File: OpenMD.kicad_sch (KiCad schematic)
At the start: 27 parts, among them J1 GND, J2 Digital, J3 Analog, J5 A, J6 B, J7 C, J8 V_{BATT}

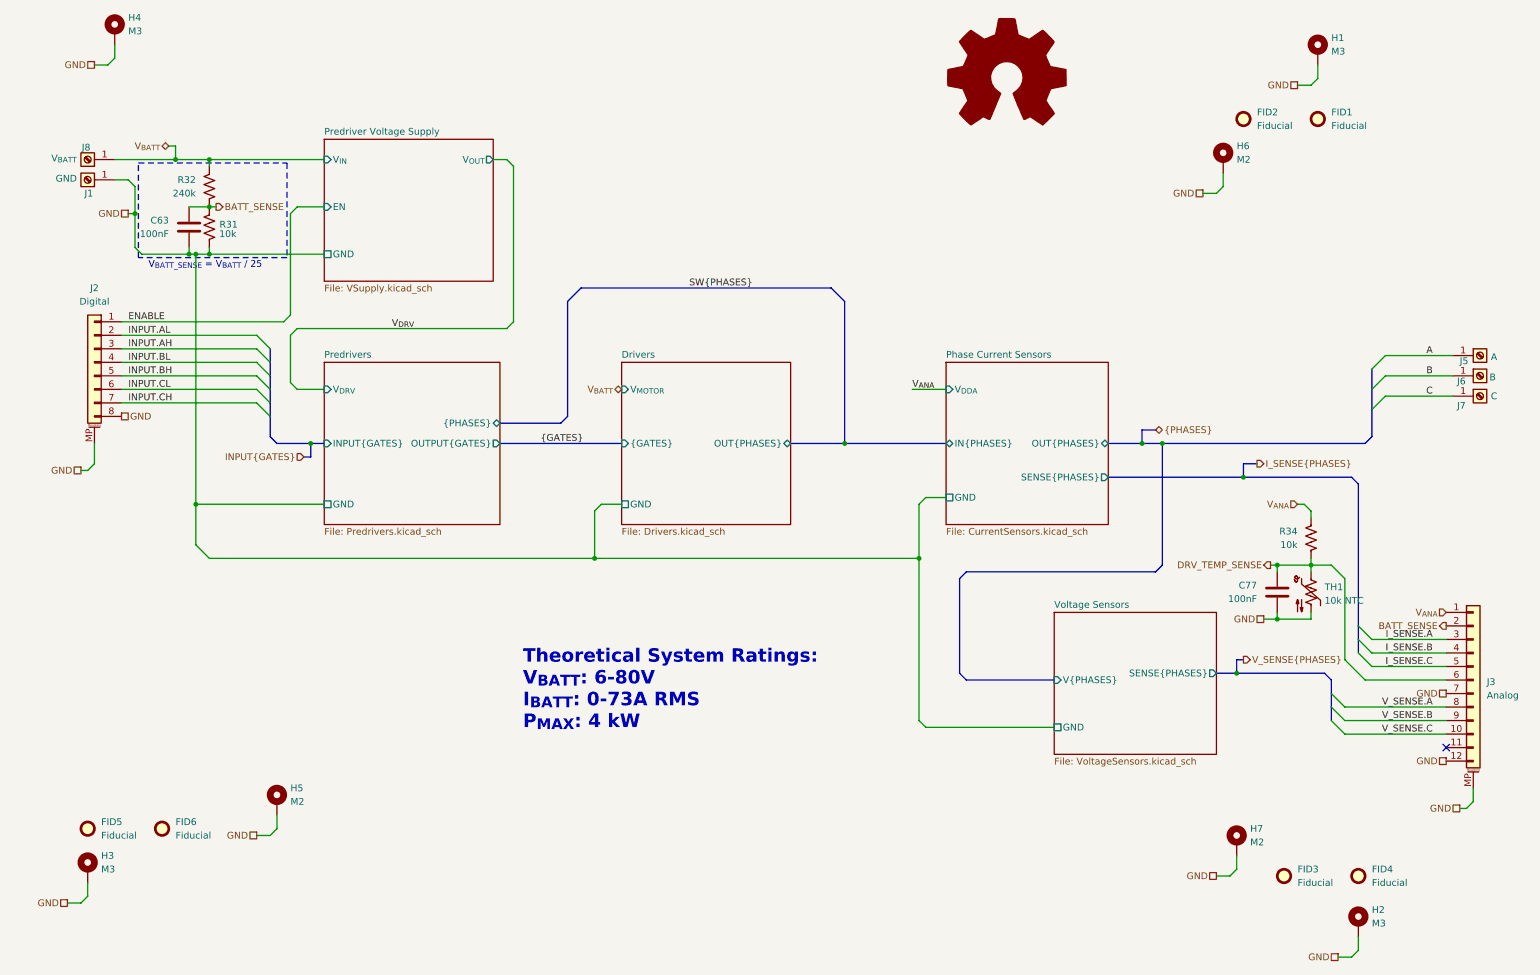
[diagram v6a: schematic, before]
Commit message: added more capacitance
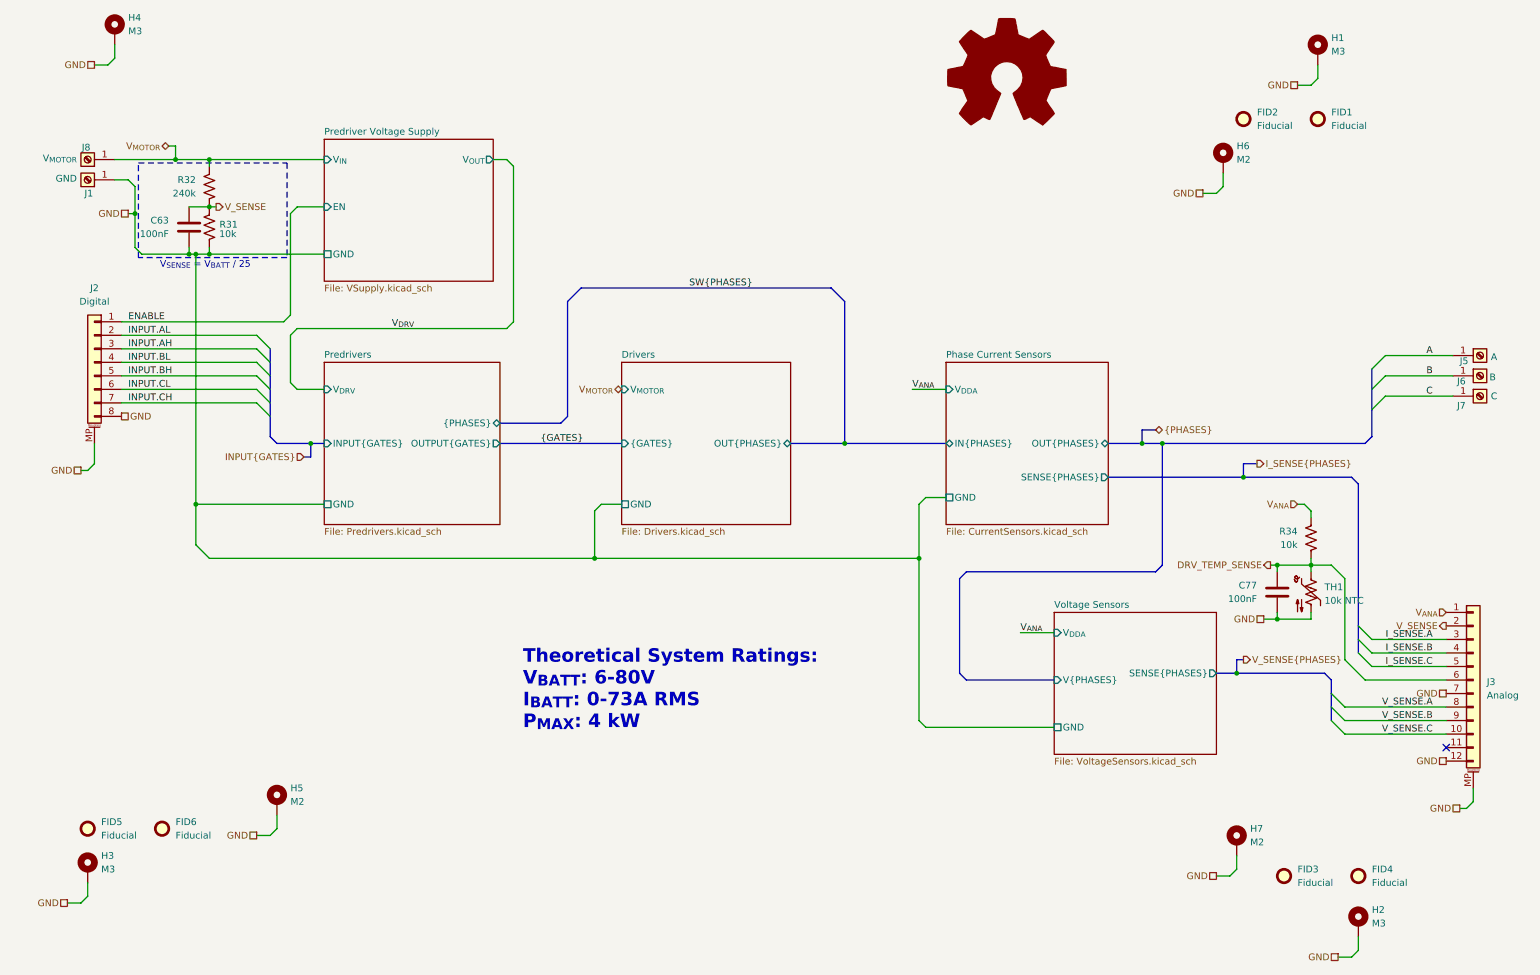
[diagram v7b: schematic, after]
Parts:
- C63, C77: footprint Capacitor_SMD:C_0402_1005Metric -> OpenMD:C_0402_1005Metric; symbol Device:C -> OpenMD:C
- FID1, FID2, FID3, FID4, FID5, FID6: symbol Mechanical:Fiducial -> OpenMD:Fiducial
- H1, H2, H3, H4, H5, H6, H7: symbol Mechanical:MountingHole_Pad -> OpenMD:MountingHole_Pad
- J1, J5, J6, J7: symbol Connector:Screw_Terminal_01x01 -> OpenMD:Screw_Terminal_01x01
- J2: footprint Connector_JST:JST_SH_SM08B-SRSS-TB_1x08-1MP_P1.00mm_Horizontal -> OpenMD:JST_SH_SM08B-SRSS-TB_1x08-1MP_P1.00mm_Horizontal; symbol Connector_Generic_MountingPin:Conn_01x08_MountingPin -> OpenMD:Conn_01x08_MountingPin
- J3: footprint Connector_JST:JST_SH_SM12B-SRSS-TB_1x12-1MP_P1.00mm_Horizontal -> OpenMD:JST_SH_SM12B-SRSS-TB_1x12-1MP_P1.00mm_Horizontal; symbol Connector_Generic_MountingPin:Conn_01x12_MountingPin -> OpenMD:Conn_01x12_MountingPin
- J8: value V_{BATT} -> V_{MOTOR}; symbol Connector:Screw_Terminal_01x01 -> OpenMD:Screw_Terminal_01x01
- R31, R32, R34: footprint Resistor_SMD:R_0402_1005Metric -> OpenMD:R_0402_1005Metric; symbol Device:R_US -> OpenMD:R_US
- SYM1: footprint Symbol:OSHW-Symbol_8.9x8mm_SilkScreen -> Symbol:OSHW-Logo2_7.3x6mm_SilkScreen; symbol Graphic:Logo_Open_Hardware_Large -> OpenMD:Logo_Open_Hardware_Large
- TH1: footprint Resistor_SMD:R_0402_1005Metric -> OpenMD:R_0402_1005Metric; symbol Device:Thermistor_NTC_US -> OpenMD:Thermistor_NTC_US
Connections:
- net BATT_SENSE renamed V_SENSE
- net V_{BATT} renamed V_{MOTOR}
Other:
- sheet Voltage Sensors ports: added V_{DDA}; removed none
- note added: "V_{SENSE} = V_{BATT} / 25"
- note removed: "V_{BATT_SENSE} = V_{BATT} / 25"
- title: 3 Phase Motor Driver -> OpenMD
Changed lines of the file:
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@@
 	(paper "A3")
 	(title_block
-		(title "3 Phase Motor Driver")
-		(date "2024-05-19")
-		(rev "1")
+		(title "OpenMD")
+		(date "2024-12-19")
+		(rev "1.1")
 		(company "Crab Labs")
 		(comment 1 "Author: Orion Serup")
@@
 	(wire
 		(pts
+			(xy 269.24 157.48) (xy 275.59 157.48)
+		)
+		(stroke
+			(width 0)
+			(type default)
+		)
+	)
+	(wire
+		(pts
 			(xy 114.3 133.35) (xy 114.3 140.97)
 		)
@@
 		)
 	)
-	(text "V_{BATT_SENSE} = V_{BATT} / 25\n"
+	(text "V_{SENSE} = V_{BATT} / 25\n"
 		(exclude_from_sim no)
 		(at 116.078 88.392 0)
@@
 		)
 	)
+	(label "V_{ANA}"
+		(at 269.24 157.48 0)
+		(fields_autoplaced yes)
+		(effects
+			(font
+				(size 1.27 1.27)
+			)
+			(justify left bottom)
+		)
+	)
 	(label "V_SENSE.A"
 		(at 346.71 171.45 180)
@@
 		)
 	)
-	(hierarchical_label "V_{BATT}"
+	(hierarchical_label "V_{MOTOR}"
 		(shape bidirectional)
 		(at 194.31 111.76 180)
@@
 		)
 	)
-	(hierarchical_label "BATT_SENSE"
+	(hierarchical_label "V_SENSE"
 		(shape output)
 		(at 349.25 156.21 180)
@@
 		)
 	)
-	(hierarchical_label "BATT_SENSE"
+	(hierarchical_label "V_SENSE"
 		(shape output)
 		(at 118.11 77.47 0)
@@
 		)
 	)
-	(hierarchical_label "V_{BATT}"
+	(hierarchical_label "V_{MOTOR}"
 		(shape bidirectional)
 		(at 109.22 66.04 180)
@@
 	)
 	(symbol
-		(lib_id "Device:R_US")
+		(lib_id "OpenMD:R_US")
 		(at 116.84 73.66 0)
 		(mirror y)
@@
 			)
 		)
-		(property "Footprint" "Resistor_SMD:R_0402_1005Metric"
+		(property "Footprint" "OpenMD:R_0402_1005Metric"
 			(at 115.824 73.914 90)
 			(effects
@@
 	)
 	(symbol
-		(lib_id "Device:C")
+		(lib_id "OpenMD:C")
 		(at 317.5 149.86 0)
 		(mirror y)
@@
 			)
 		)
-		(property "Footprint" "Capacitor_SMD:C_0402_1005Metric"
+		(property "Footprint" "OpenMD:C_0402_1005Metric"
 			(at 316.5348 153.67 0)
 			(effects
@@
 	)
 	(symbol
-		(lib_id "Graphic:Logo_Open_Hardware_Large")
+		(lib_id "OpenMD:Logo_Open_Hardware_Large")
 		(at 266.7 53.34 0)
 		(unit 1)
@@
 			)
 		)
-		(property "Footprint" "Symbol:OSHW-Symbol_8.9x8mm_SilkScreen"
+		(property "Footprint" "Symbol:OSHW-Logo2_7.3x6mm_SilkScreen"
 			(at 266.7 53.34 0)
 			(effects
@@
 	)
 	(symbol
-		(lib_id "Mechanical:MountingHole_Pad")
+		(lib_id "OpenMD:MountingHole_Pad")
 		(at 93.98 201.93 0)
 		(unit 1)
@@
 	)
 	(symbol
-		(lib_id "Mechanical:MountingHole_Pad")
+		(lib_id "OpenMD:MountingHole_Pad")
 		(at 325.12 48.26 0)
 		(unit 1)
@@
 	)
 	(symbol
-		(lib_id "Mechanical:Fiducial")
+		(lib_id "OpenMD:Fiducial")
 		(at 93.98 194.31 0)
 		(unit 1)
@@
 	)
 	(symbol
-		(lib_id "Connector:Screw_Terminal_01x01")
+		(lib_id "OpenMD:Screw_Terminal_01x01")
 		(at 93.98 72.39 180)
 		(unit 1)
@@
 	)
 	(symbol
-		(lib_id "Connector:Screw_Terminal_01x01")
+		(lib_id "OpenMD:Screw_Terminal_01x01")
 		(at 355.6 105.41 0)
 		(unit 1)
@@
 	)
 	(symbol
-		(lib_id "Connector_Generic_MountingPin:Conn_01x08_MountingPin")
+		(lib_id "OpenMD:Conn_01x08_MountingPin")
 		(at 95.25 106.68 0)
 		(mirror y)
@@
 			)
 		)
-		(property "Footprint" "Connector_JST:JST_SH_SM08B-SRSS-TB_1x08-1MP_P1.00mm_Horizontal"
+		(property "Footprint" "OpenMD:JST_SH_SM08B-SRSS-TB_1x08-1MP_P1.00mm_Horizontal"
 			(at 95.25 106.68 0)
 			(effects
@@
 	)
 	(symbol
-		(lib_id "Mechanical:MountingHole_Pad")
+		(lib_id "OpenMD:MountingHole_Pad")
 		(at 332.74 212.09 0)
 		(unit 1)
@@
 	)
 	(symbol
-		(lib_id "Mechanical:Fiducial")
+		(lib_id "OpenMD:Fiducial")
 		(at 311.15 60.96 0)
 		(unit 1)
@@
 	)
 	(symbol
-		(lib_id "Mechanical:Fiducial")
+		(lib_id "OpenMD:Fiducial")
 		(at 325.12 60.96 0)
 		(unit 1)
@@
 	)
 	(symbol
-		(lib_id "Connector_Generic_MountingPin:Conn_01x12_MountingPin")
+		(lib_id "OpenMD:Conn_01x12_MountingPin")
 		(at 354.33 166.37 0)
 		(unit 1)
@@
 			)
 		)
-		(property "Footprint" "Connector_JST:JST_SH_SM12B-SRSS-TB_1x12-1MP_P1.00mm_Horizontal"
+		(property "Footprint" "OpenMD:JST_SH_SM12B-SRSS-TB_1x12-1MP_P1.00mm_Horizontal"
 			(at 354.33 166.37 0)
 			(effects
@@
 	)
 	(symbol
-		(lib_id "Device:R_US")
+		(lib_id "OpenMD:R_US")
 		(at 116.84 81.28 0)
 		(mirror y)
@@
 			)
 		)
-		(property "Footprint" "Resistor_SMD:R_0402_1005Metric"
+		(property "Footprint" "OpenMD:R_0402_1005Metric"
 			(at 115.824 81.534 90)
 			(effects
@@
 	)
 	(symbol
-		(lib_id "Device:R_US")
+		(lib_id "OpenMD:R_US")
 		(at 323.85 139.7 0)
 		(mirror y)
@@
 			)
 		)
-		(property "Footprint" "Resistor_SMD:R_0402_1005Metric"
+		(property "Footprint" "OpenMD:R_0402_1005Metric"
 			(at 322.834 139.954 90)
 			(effects
@@
 	)
 	(symbol
-		(lib_id "Mechanical:Fiducial")
+		(lib_id "OpenMD:Fiducial")
 		(at 107.95 194.31 0)
 		(unit 1)
@@
 	)
 	(symbol
-		(lib_id "Mechanical:MountingHole_Pad")
+		(lib_id "OpenMD:MountingHole_Pad")
 		(at 129.54 189.23 0)
 		(unit 1)
@@
 	)
 	(symbol
-		(lib_id "Mechanical:MountingHole_Pad")
+		(lib_id "OpenMD:MountingHole_Pad")
 		(at 307.34 68.58 0)
 		(unit 1)
@@
 	)
 	(symbol
-		(lib_id "Device:Thermistor_NTC_US")
+		(lib_id "OpenMD:Thermistor_NTC_US")
 		(at 323.85 149.86 0)
 		(unit 1)
@@
 			)
 		)
-		(property "Footprint" "Resistor_SMD:R_0402_1005Metric"
+		(property "Footprint" "OpenMD:R_0402_1005Metric"
 			(at 323.85 148.59 0)
 			(effects
@@
 	)
 	(symbol
-		(lib_id "Mechanical:Fiducial")
+		(lib_id "OpenMD:Fiducial")
 		(at 332.74 203.2 0)
 		(unit 1)
@@
 	)
 	(symbol
-		(lib_id "Mechanical:Fiducial")
+		(lib_id "OpenMD:Fiducial")
 		(at 318.77 203.2 0)
 		(unit 1)
@@
 	)
 	(symbol
-		(lib_id "Connector:Screw_Terminal_01x01")
+		(lib_id "OpenMD:Screw_Terminal_01x01")
 		(at 355.6 109.22 0)
 		(unit 1)
@@
 	)
 	(symbol
-		(lib_id "Mechanical:MountingHole_Pad")
+		(lib_id "OpenMD:MountingHole_Pad")
 		(at 309.88 196.85 0)
 		(unit 1)
@@
 	)
 	(symbol
-		(lib_id "Connector:Screw_Terminal_01x01")
+		(lib_id "OpenMD:Screw_Terminal_01x01")
 		(at 93.98 68.58 180)
 		(unit 1)
@@
 			)
 		)
-		(property "Value" "V_{BATT}"
+		(property "Value" "V_{MOTOR}"
 			(at 91.948 68.326 0)
 			(effects
@@
 	)
 	(symbol
-		(lib_id "Device:C")
+		(lib_id "OpenMD:C")
 		(at 113.03 81.28 0)
 		(mirror y)
@@
 			)
 		)
-		(property "Footprint" "Capacitor_SMD:C_0402_1005Metric"
+		(property "Footprint" "OpenMD:C_0402_1005Metric"
 			(at 112.0648 85.09 0)
 			(effects
@@
 	)
 	(symbol
-		(lib_id "Mechanical:MountingHole_Pad")
+		(lib_id "OpenMD:MountingHole_Pad")
 		(at 99.06 44.45 0)
 		(unit 1)
@@
 	)
 	(symbol
-		(lib_id "Connector:Screw_Terminal_01x01")
+		(lib_id "OpenMD:Screw_Terminal_01x01")
 		(at 355.6 113.03 0)
 		(unit 1)
@@
 			(effects
 				(font
+					(size 1.27 1.27)
+				)
+				(justify left)
+			)
+		)
+		(pin "V_{DDA}" input
+			(at 275.59 157.48 180)
+			(effects
+				(font
